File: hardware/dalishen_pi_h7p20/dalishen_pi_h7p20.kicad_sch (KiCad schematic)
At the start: 104 parts, among them J1 Conn_02x05_Odd_Even, J6 5V, J7 OV5640, J9 D500C930SV0, SW1 SW_Push, SW2 SW_Push, SW3 SW_DIP_x03, SW4 SW_Push, SW5 SW_Push, U3 H7P20N0L128-M3H1, U4 SY7201ABC, U5 XC6206-2.8, U7 P25Q32SH-SSH-IT, U8 XC6206-1.5, X1 NC

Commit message: [dalishen_pi_h7p20] 样板
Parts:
- C4, C41: value NC -> 10uF
- U7: value P25Q32SH-SSH-IT -> P25Q64SH-SSH-IR
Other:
- note added: "OV/TP_SCL：可置0或高阻 OV/TP_SDA：可置0或高阻"
- note removed: "OV/TP_SCL：可置0或高阻 OV/TP_SDA：可置0或高阻 OV_PWDN：可置0或高阻"
- moved on the sheet: C72, C73, C74, C75, C76, C77, J7, R11, R68, R69, R9, U5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

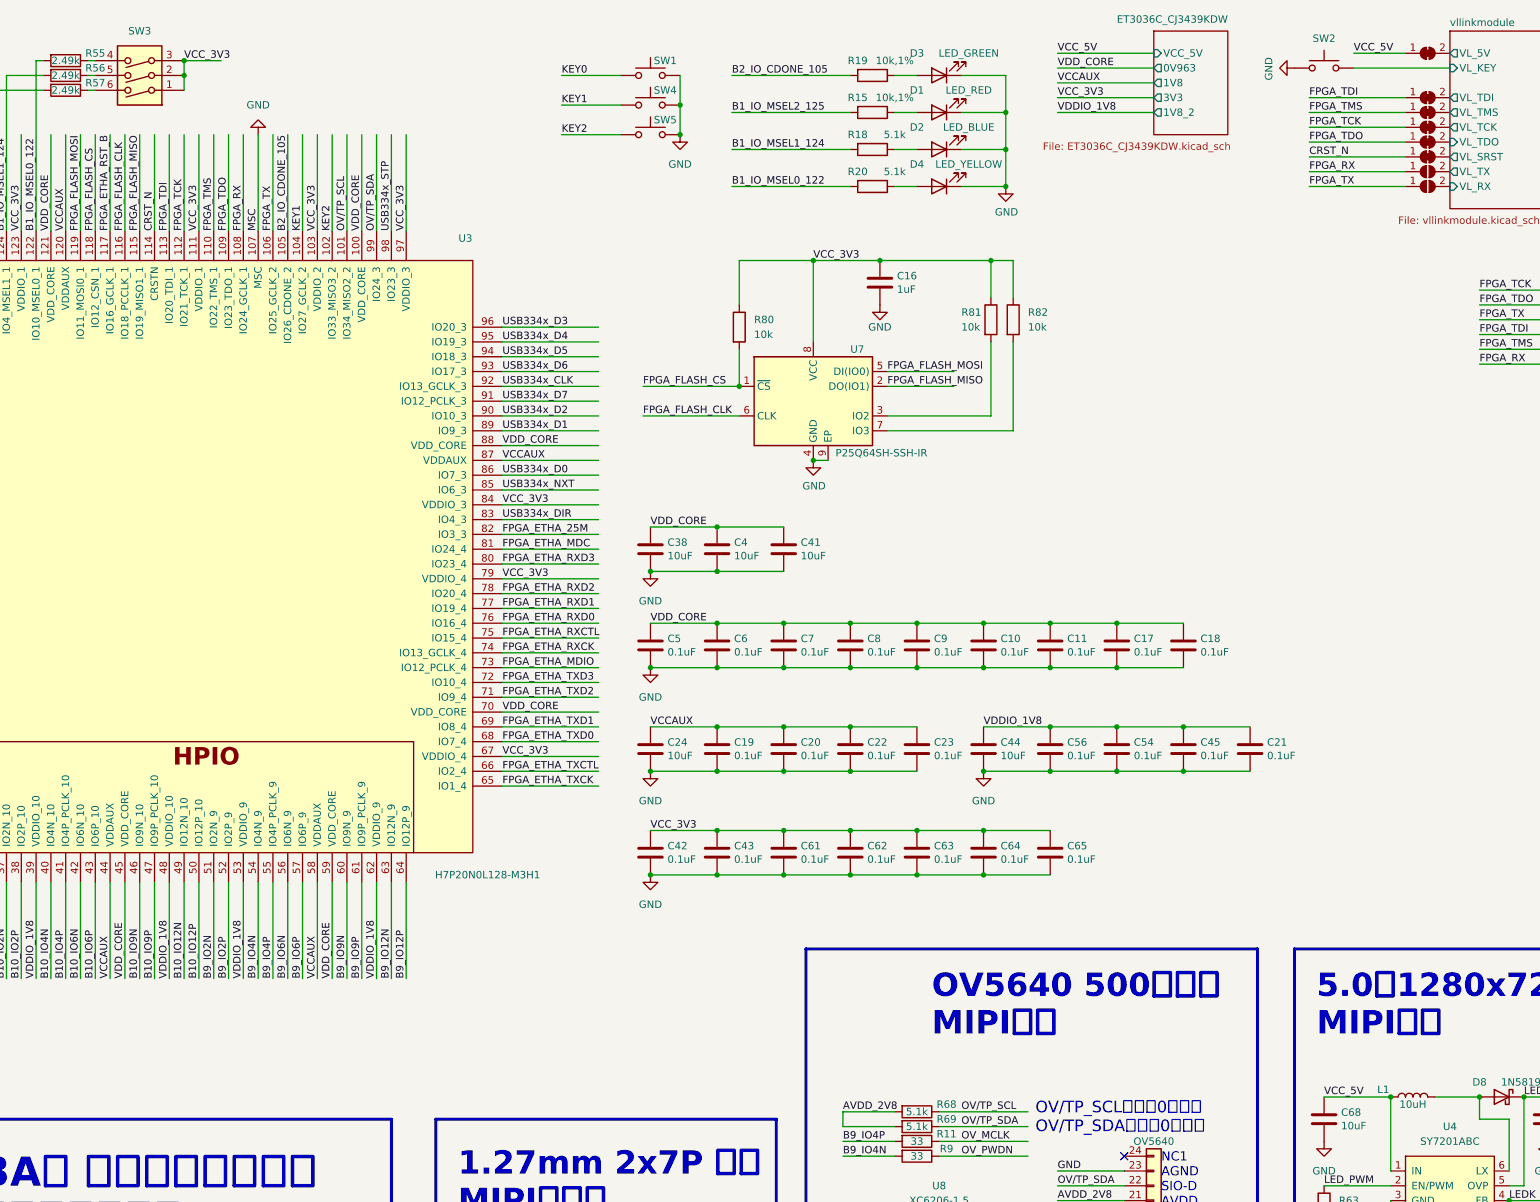
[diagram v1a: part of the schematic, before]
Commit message: [dalishen_pi_h7p20] YT8531C需增加一个电感；需从XO引入时钟，XI接地； 剩余样板需换贴YC8531DC或者手工割线加电感。千兆协商通过。 LAYOUT优化
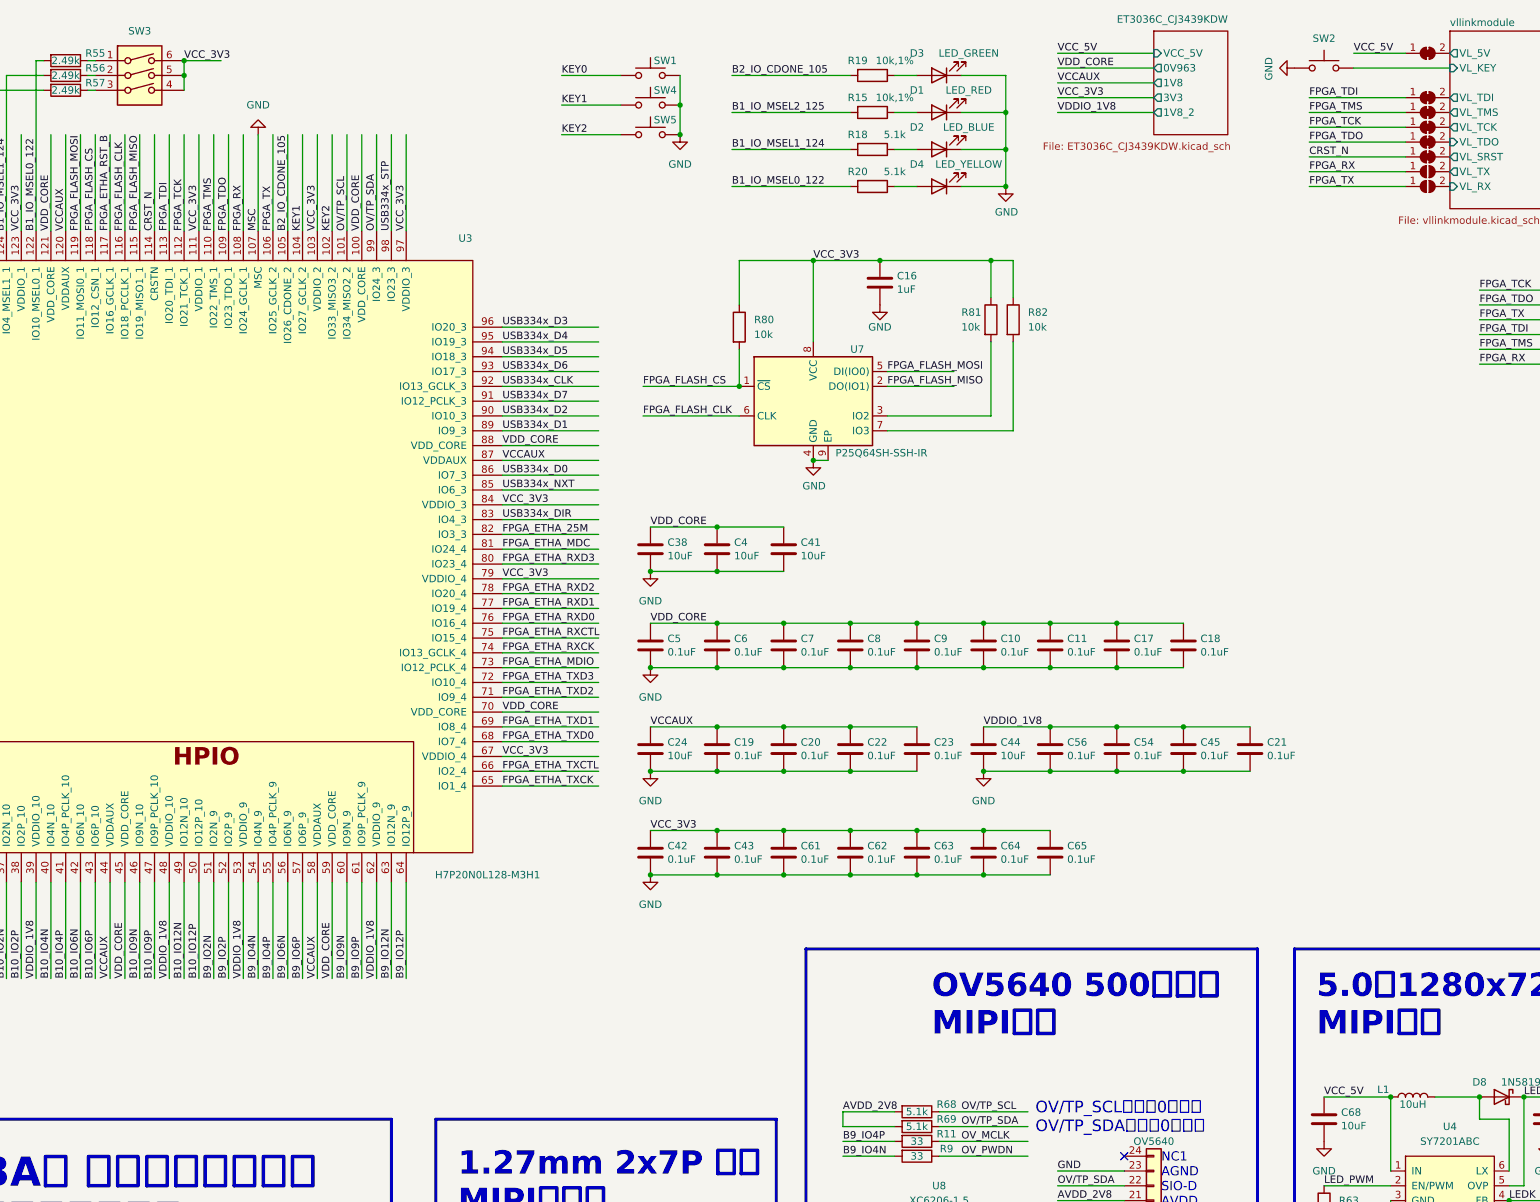
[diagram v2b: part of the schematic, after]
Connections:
- net VCC_3V3: now also SW3.4, SW3.5, SW3.6; no longer SW3.1, SW3.2, SW3.3
- net at R57.1: now also SW3.3; no longer SW3.6
- net at R56.1: now also SW3.2; no longer SW3.5
- net at R55.1: now also SW3.1; no longer SW3.4
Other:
- moved on the sheet: SW3

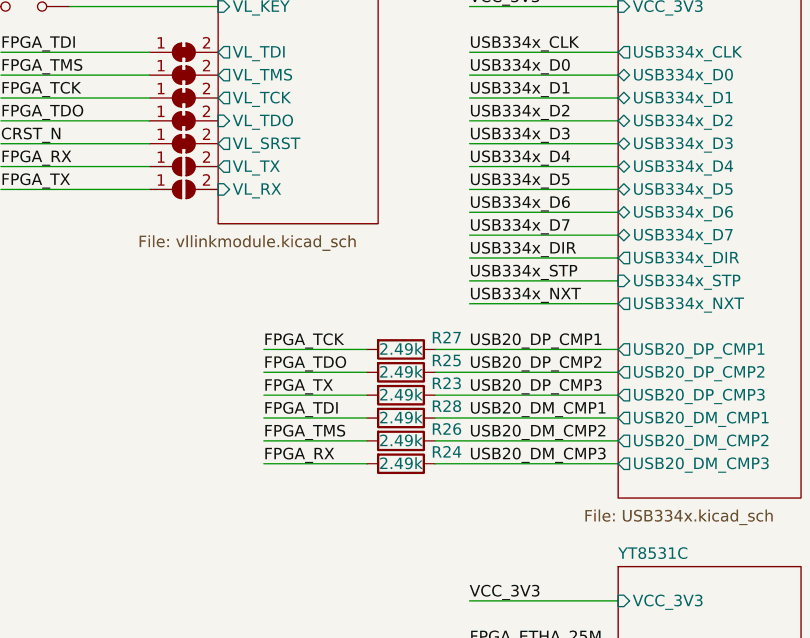
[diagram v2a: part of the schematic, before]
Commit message: [dalishen_pi_h7p20] 由于JTAG口在LQFP128封装上无法作为IO使用，故移除SE0，J, K状态电路
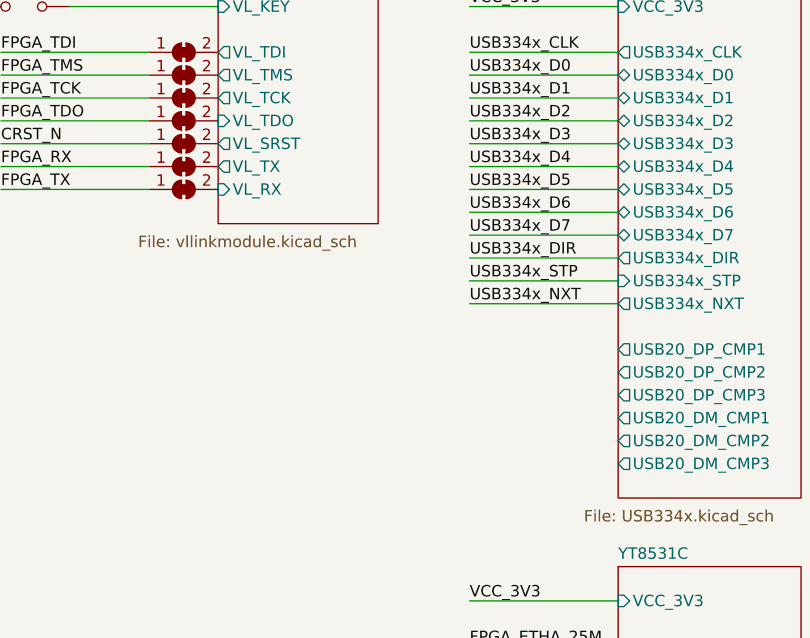
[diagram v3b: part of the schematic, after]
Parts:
- removed JP1, JP10: SolderJumper_2_Open, Jumper:SolderJumper-2_P1.3mm_Open_RoundedPad1.0x1.5mm, symbol Jumper:SolderJumper_2_Open
- removed R23, R24, R25, R26, R27, R28: 2.49k, Resistor_SMD:R_0402_1005Metric, symbol Device:R
- added JP7, JP8: SolderJumper_2_Bridged, Jumper:SolderJumper-2_P1.3mm_Bridged_RoundedPad1.0x1.5mm, symbol Jumper:SolderJumper_2_Bridged
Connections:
- net FPGA_RX: now also JP7.1 (A)
- net FPGA_TX: now also JP8.1 (A)
- net vllinkmodule/VL_RX: now also JP8.2 (B)
- net vllinkmodule/VL_TX: now also JP7.2 (B)

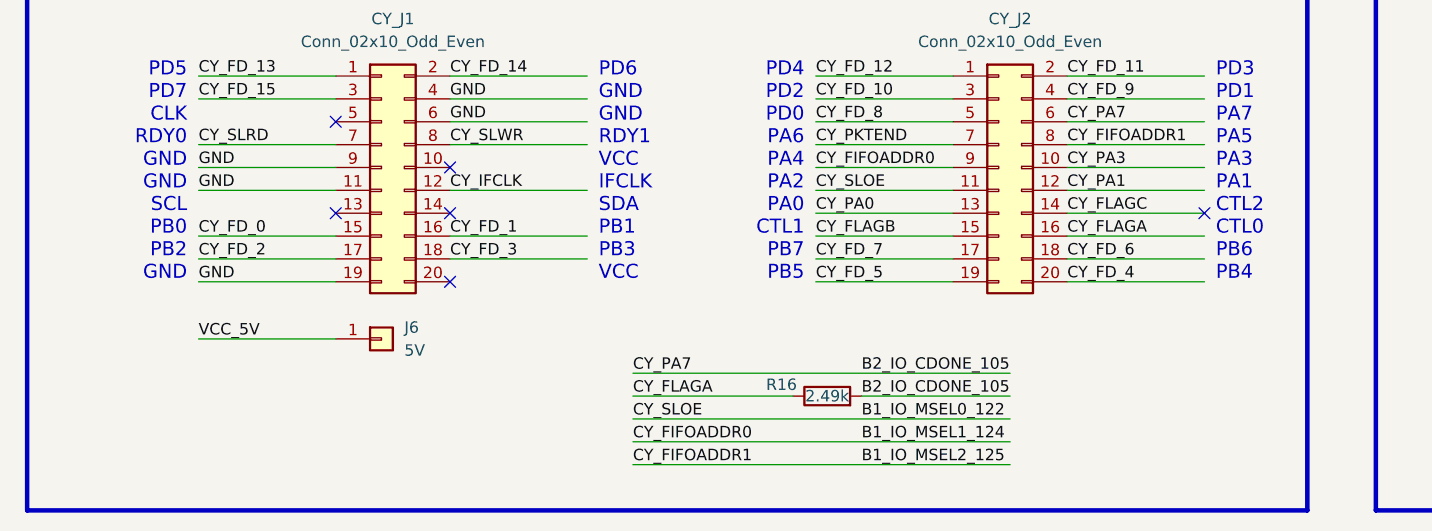
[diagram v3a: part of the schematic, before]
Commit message: [dalishen_pi_h7p20] 两个双排针的VCC脚通过短接点连接3.3V，预留给其他扩展模块供电的能力。
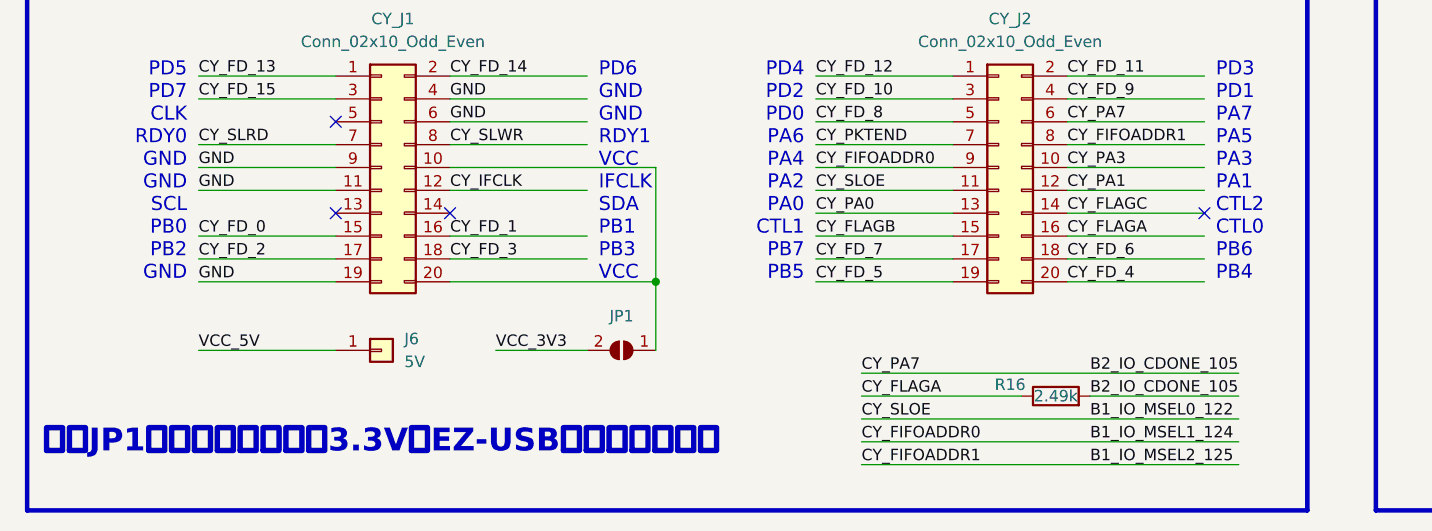
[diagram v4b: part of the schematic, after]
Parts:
- added JP1: SolderJumper_2_Open, Jumper:SolderJumper-2_P1.3mm_Open_RoundedPad1.0x1.5mm, symbol Jumper:SolderJumper_2_Open
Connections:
- net VCC_3V3: now also JP1.2 (B)
- net at CY_J1.10 (Pin_10): now also CY_J1.20 (Pin_20), JP1.1 (A)
- no-connect marks 18 -> 16
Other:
- note added: "注：JP1短接后可对外输出3.3V。EZ-USB板不需要短接。"
- moved on the sheet: J6, R16
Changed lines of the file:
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@@
 		)
 	)
+	(text "注：JP1短接后可对外输出3.3V。EZ-USB板不需要短接。"
+		(exclude_from_sim no)
+		(at 17.018 275.844 0)
+		(effects
+			(font
+				(face "仿宋")
+				(size 2.54 2.54)
+				(thickness 0.6)
+				(bold yes)
+			)
+			(justify left bottom)
+		)
+	)
 	(text "NC1\nAGND\nSIO-D\nAVDD\nSIO-C\nRESET\nNC\nPWDN\nNC\nDVDD\nDOVDD\nMDP1\nMCLK\nMDN1\nDGND\nMCP\nNC\nMCN\nNC\nMDP0\nNC\nMDN0\nAF-VDD\nNC"
 		(exclude_from_sim no)
@@
 	)
 	(junction
+		(at 85.09 256.54)
+		(diameter 0)
+		(color 0 0 0 0)
+	)
+	(junction
 		(at 317.5 222.25)
 		(diameter 0)
@@
 	)
 	(no_connect
-		(at 62.23 243.84)
-	)
-	(no_connect
 		(at 386.08 189.23)
 	)
@@
 		(at 283.21 224.79)
 	)
-	(no_connect
-		(at 62.23 256.54)
-	)
 	(wire
 		(pts
@@
 	(wire
 		(pts
-			(xy 82.55 266.7) (xy 124.46 266.7)
+			(xy 107.95 266.7) (xy 149.86 266.7)
 		)
 		(stroke
@@
 	(wire
 		(pts
+			(xy 85.09 264.16) (xy 85.09 256.54)
+		)
+		(stroke
+			(width 0)
+			(type default)
+		)
+	)
+	(wire
+		(pts
 			(xy 193.04 87.63) (xy 176.53 87.63)
 		)
@@
 	(wire
 		(pts
-			(xy 34.29 262.89) (xy 49.53 262.89)
+			(xy 34.29 264.16) (xy 49.53 264.16)
 		)
 		(stroke
@@
 	(wire
 		(pts
+			(xy 85.09 256.54) (xy 62.23 256.54)
+		)
+		(stroke
+			(width 0)
+			(type default)
+		)
+	)
+	(wire
+		(pts
 			(xy 54.61 29.21) (xy 54.61 30.48)
 		)
@@
 	(wire
 		(pts
-			(xy 82.55 271.78) (xy 124.46 271.78)
+			(xy 107.95 271.78) (xy 149.86 271.78)
 		)
 		(stroke
@@
 	(wire
 		(pts
-			(xy 82.55 269.24) (xy 100.33 269.24)
+			(xy 107.95 269.24) (xy 125.73 269.24)
 		)
 		(stroke
@@
 	(wire
 		(pts
+			(xy 85.09 256.54) (xy 85.09 243.84)
+		)
+		(stroke
+			(width 0)
+			(type default)
+		)
+	)
+	(wire
+		(pts
 			(xy 186.69 34.29) (xy 196.85 34.29)
 		)
@@
 	(wire
 		(pts
+			(xy 62.23 243.84) (xy 85.09 243.84)
+		)
+		(stroke
+			(width 0)
+			(type default)
+		)
+	)
+	(wire
+		(pts
 			(xy 193.04 130.81) (xy 176.53 130.81)
 		)
@@
 	(wire
 		(pts
-			(xy 82.55 276.86) (xy 124.46 276.86)
+			(xy 107.95 276.86) (xy 149.86 276.86)
 		)
 		(stroke
@@
 	(wire
 		(pts
-			(xy 107.95 269.24) (xy 124.46 269.24)
+			(xy 133.35 269.24) (xy 149.86 269.24)
 		)
 		(stroke
@@
 	(wire
 		(pts
-			(xy 82.55 274.32) (xy 124.46 274.32)
+			(xy 107.95 274.32) (xy 149.86 274.32)
 		)
 		(stroke
@@
 	(wire
 		(pts
+			(xy 67.31 264.16) (xy 77.47 264.16)
+		)
+		(stroke
+			(width 0)
+			(type default)
+		)
+	)
+	(wire
+		(pts
 			(xy 383.54 139.7) (xy 367.03 139.7)
 		)
@@
 	)
 	(label "CY_PA7"
-		(at 82.55 266.7 0)
+		(at 107.95 266.7 0)
 		(effects
 			(font
@@
 	)
 	(label "B2_IO_CDONE_105"
-		(at 107.95 266.7 0)
+		(at 133.35 266.7 0)
 		(effects
 			(font
@@
 	)
 	(label "B1_IO_MSEL2_125"
-		(at 107.95 276.86 0)
+		(at 133.35 276.86 0)
 		(effects
 			(font
@@
 	)
 	(label "B2_IO_CDONE_105"
-		(at 107.95 269.24 0)
+		(at 133.35 269.24 0)
 		(effects
 			(font
@@
 	)
 	(label "VCC_5V"
-		(at 34.29 262.89 0)
+		(at 34.29 264.16 0)
 		(effects
 			(font
@@
 	)
 	(label "CY_FIFOADDR0"
-		(at 82.55 274.32 0)
+		(at 107.95 274.32 0)
 		(effects
 			(font
@@
 	)
 	(label "B1_IO_MSEL1_124"
-		(at 107.95 274.32 0)
+		(at 133.35 274.32 0)
 		(effects
 			(font
@@
 		)
 	)
+	(label "VCC_3V3"
+		(at 67.31 264.16 0)
+		(effects
+			(font
+				(size 1.27 1.27)
+			)
+			(justify left bottom)
+		)
+	)
 	(label "USB334x_STP"
 		(at 367.03 53.34 0)
@@
 	)
 	(label "B1_IO_MSEL0_122"
-		(at 107.95 271.78 0)
+		(at 133.35 271.78 0)
 		(effects
 			(font
@@
 	)
 	(label "CY_FIFOADDR1"
-		(at 82.55 276.86 0)
+		(at 107.95 276.86 0)
 		(effects
 			(font
@@
 	)
 	(label "CY_FLAGA"
-		(at 82.55 269.24 0)
+		(at 107.95 269.24 0)
 		(effects
 			(font
@@
 	)
 	(label "CY_SLOE"
-		(at 82.55 271.78 0)
+		(at 107.95 271.78 0)
 		(effects
 			(font
@@
 	(symbol
 		(lib_id "Connector_Generic:Conn_01x01")
-		(at 54.61 262.89 0)
+		(at 54.61 264.16 0)
 		(unit 1)
 		(exclude_from_sim no)
@@
 		(dnp no)
 		(property "Reference" "J6"
-			(at 57.15 261.62 0)
+			(at 57.15 262.89 0)
 			(effects
 				(font
@@
 		)
 		(property "Value" "5V"
-			(at 57.15 264.16 0)
+			(at 57.15 265.43 0)
 			(effects
 				(font
@@
 		)
 		(property "Footprint" "Connector_PinHeader_2.54mm:PinHeader_1x01_P2.54mm_Horizontal"
-			(at 54.61 262.89 0)
+			(at 54.61 264.16 0)
 			(effects
 				(font
@@
 		)
 		(property "Datasheet" "~"
-			(at 54.61 262.89 0)
+			(at 54.61 264.16 0)
 			(effects
 				(font
@@
 		)
 		(property "Description" ""
-			(at 54.61 262.89 0)
+			(at 54.61 264.16 0)
 			(effects
 				(font
@@
 	(symbol
 		(lib_id "Device:R")
-		(at 104.14 269.24 90)
+		(at 129.54 269.24 90)
 		(unit 1)
 		(exclude_from_sim no)
@@
 		(dnp no)
 		(property "Reference" "R16"
-			(at 99.06 267.97 90)
+			(at 124.46 267.97 90)
 			(effects
 				(font
@@
 		)
 		(property "Value" "2.49k"
-			(at 104.14 269.24 90)
+			(at 129.54 269.24 90)
 			(effects
 				(font
@@
 		)
 		(property "Footprint" "Resistor_SMD:R_0402_1005Metric"
-			(at 104.14 271.018 90)
+			(at 129.54 271.018 90)
 			(effects
 				(font
@@
 		)
 		(property "Datasheet" "~"
-			(at 104.14 269.24 0)
+			(at 129.54 269.24 0)
 			(effects
 				(font
@@
 		)
 		(property "Description" ""
-			(at 104.14 269.24 0)
+			(at 129.54 269.24 0)
 			(effects
 				(font
@@
 					(unit 1)
 				)
+			)
+		)
+	)
+	(symbol
+		(lib_id "Jumper:SolderJumper_2_Open")
+		(at 81.28 264.16 180)
+		(unit 1)
+		(exclude_from_sim no)
+		(in_bom no)
+		(on_board yes)
+		(dnp no)
+		(fields_autoplaced yes)
+		(property "Reference" "JP1"
+			(at 81.28 260.35 0)
+			(effects
+				(font
+					(size 1.27 1.27)
+				)
+			)
+		)
+		(property "Value" "SolderJumper_2_Open"
+			(at 81.28 267.97 0)
+			(effects
+				(font
+					(size 1.27 1.27)
+				)
+				(hide yes)
+			)
+		)
+		(property "Footprint" "Jumper:SolderJumper-2_P1.3mm_Open_RoundedPad1.0x1.5mm"
+			(at 81.28 264.16 0)
+			(effects
+				(font
+					(size 1.27 1.27)
+				)
+				(hide yes)
+			)
+		)
+		(property "Datasheet" "~"
+			(at 81.28 264.16 0)
+			(effects
+				(font
+					(size 1.27 1.27)
+				)
+				(hide yes)
+			)
+		)
+		(property "Description" "Solder Jumper, 2-pole, open"
+			(at 81.28 264.16 0)
+			(effects
+				(font
+					(size 1.27 1.27)
+				)
+				(hide yes)
+			)
+		)
+		(pin "2"
+		)
+		(pin "1"
+		)
+		(instances
+			(project ""
+				(path "/221176f3-b6da-4f04-afa6-f8c6dd49907a"
+					(reference "JP1")
+					(unit 1)
+				)

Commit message: [dalishen_pi_h7p20] 优化LAYOUT
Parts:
- J6: footprint Connector_PinHeader_2.54mm:PinHeader_1x01_P2.54mm_Horizontal -> Connector_PinSocket_2.54mm:PinSocket_1x01_P2.54mm_Vertical
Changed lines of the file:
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@@
 			)
 		)
-		(property "Footprint" "Connector_PinHeader_2.54mm:PinHeader_1x01_P2.54mm_Horizontal"
+		(property "Footprint" "Connector_PinSocket_2.54mm:PinSocket_1x01_P2.54mm_Vertical"
 			(at 54.61 264.16 0)
 			(effects
